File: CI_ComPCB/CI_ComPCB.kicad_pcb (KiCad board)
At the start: 2 copper layers, 101.6 x 86.4 mm, 52 parts, among them IC301 TPS63020DSJR, IC401 TPS54331DR, J101 Conn_01x01_Male, J301 Connector_Conn_01x02_Male, J302 Connector_Conn_01x02_Male, J401 Connector_Conn_01x02_Male, J402 Connector_Conn_01x02_Male, J501 RJ45_LED_Shielded, J502 RJ45_LED_Shielded, Q201 Transistor_FET_IRF9540N, U101 ESP32s

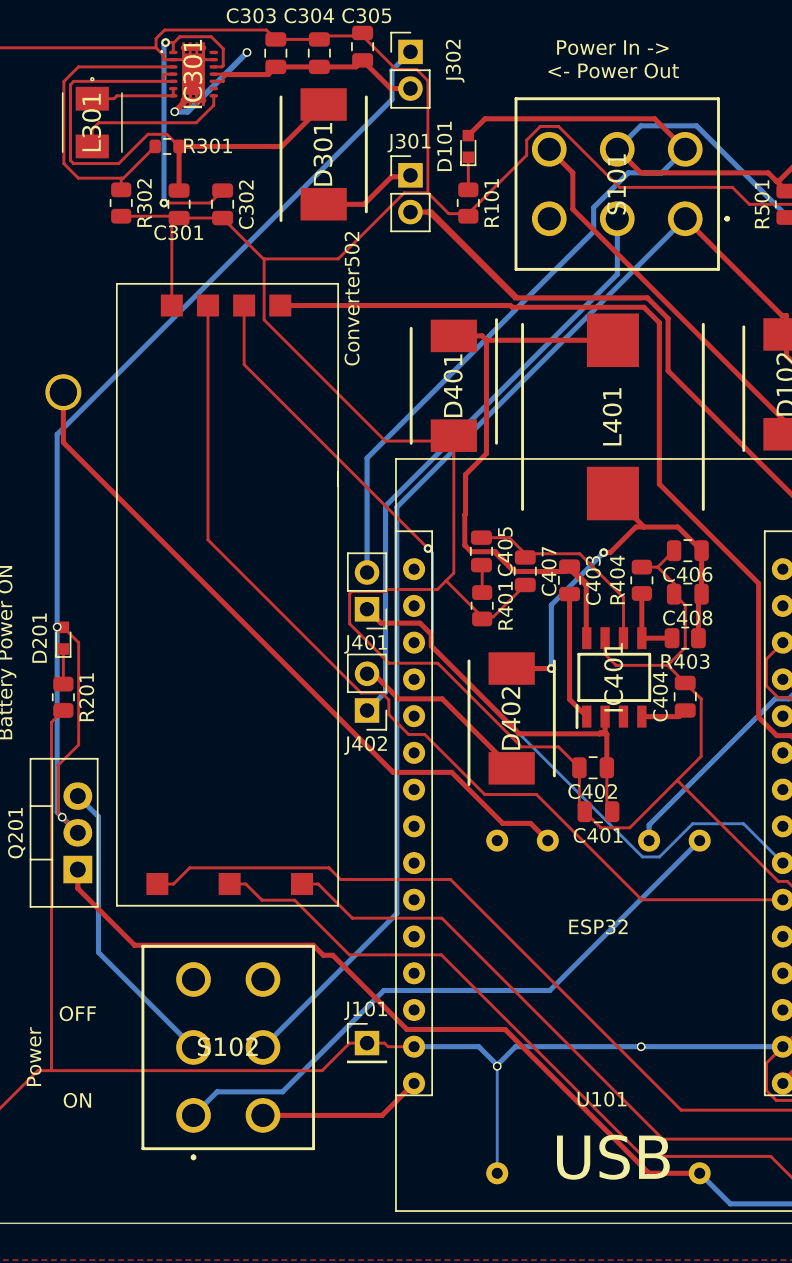
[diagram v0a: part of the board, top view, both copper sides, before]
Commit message: V1.1 board
Board is ready to print
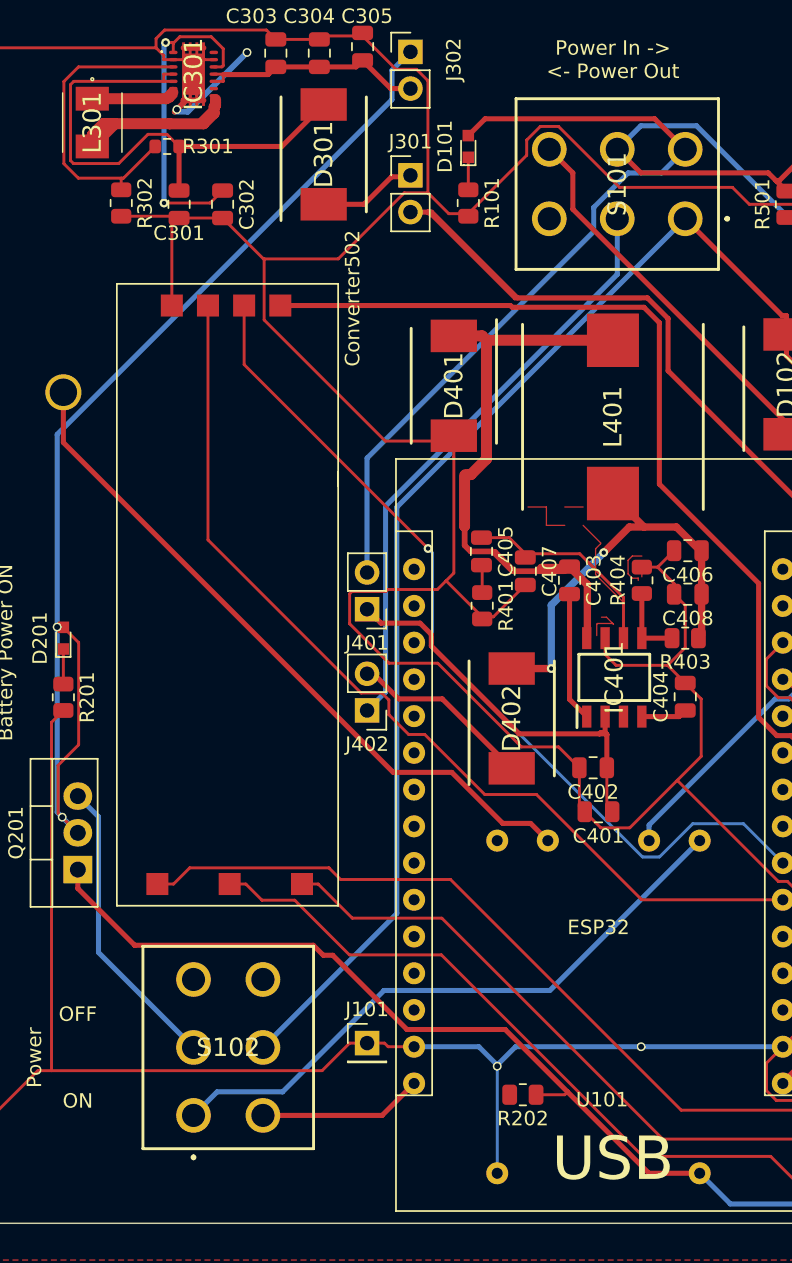
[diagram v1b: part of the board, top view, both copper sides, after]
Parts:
- added R202: 10k, Resistor_SMD:R_0805_2012Metric, F.Cu at (88.8, 151.6)
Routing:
- net Net-(IC301-Pad8): track 10.9 -> 32.9 mm
- net Net-(C403-Pad1): track 57.6 -> 74.4 mm
- net (no net): track 0.00 -> 11.1 mm
- net Net-(C405-Pad1): track 14.6 -> 21.4 mm
- net Net-(IC301-Pad6): track 6.18 -> 11.9 mm
- net Charger_IN: track 128.0 -> 130.2 mm
- net GND: track 448.1 -> 448.8 mm

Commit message: V1.1 Changed Diode for reprint
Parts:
- D102, D301, D401, D402: footprint SamacSys_Parts:DIOM8059X256N -> digikey-footprints:DO-214AC
- moved D402 2.00 mm to (89.7, 126.6)
- moved D401 1.29 mm to (83.7, 103.8)
- moved D301 0.97 mm to (74.8, 87.5)
- moved D102 0.40 mm to (107.2, 102.8)
- moved R404 0.21 mm to (97.1, 116.2)
- moved IC401 0.09 mm to (95.1, 122.8)
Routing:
- net GND: track 448.8 -> 433.6 mm, vias 6 -> 8
- net (no net): track 11.1 -> 0.00 mm
- net Net-(C405-Pad1): track 21.4 -> 14.2 mm
- net Net-(C403-Pad1): track 74.4 -> 80.0 mm
- net Net-(D402-Pad1): track 12.7 -> 14.6 mm
- net Net-(C301-Pad1): track 36.6 -> 35.4 mm
- net Net-(C401-Pad1): track 27.8 -> 28.4 mm
- net Charger_OUT: vias 2 -> 1

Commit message: converters debug
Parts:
- added Q501: Transistor_FET_IRF9540N-CI_ComPCB-cache, Package_TO_SOT_THT:TO-220-3_Vertical, F.Cu at (-2.06, 105.6)
- added Q502: Transistor_FET_IRF9540N-CI_ComPCB-cache, Package_TO_SOT_THT:TO-220-3_Vertical, F.Cu at (-2.06, 111.6)
- added R503: 10k, Resistor_SMD:R_0805_2012Metric, F.Cu at (8.46, 103.1)
- C303, C304, C305: value 100nF -> 10uf
- moved D301 40.7 mm to (52.6, 53.4), turned to 0 degrees
- moved C302 37.2 mm to (66.3, 52.9), turned to 0 degrees
- moved C301 31.3 mm to (58.4, 59.4), turned to 0 degrees
- moved R302 28.7 mm to (67.3, 61.9), turned to 0 degrees
- moved IC301 27.0 mm to (60.4, 54.6), turned to 0 degrees
- moved L301 26.3 mm to (52.7, 58.8), turned to 0 degrees
- moved C304 25.1 mm to (66.3, 55.9), turned to 0 degrees
- moved R301 24.6 mm to (58.2, 62.1)
- moved C305 22.7 mm to (67.3, 58.9), turned to 0 degrees
- moved C303 22.0 mm to (62.8, 59.4), turned to 0 degrees
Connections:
- D301 pad 2: Net-(C301-Pad1) -> Net-(C303-Pad1)
- IC301 pad 10: Net-(C303-Pad1) -> Net-(C301-Pad1)
- IC301 pad 11: Net-(C303-Pad1) -> Net-(C301-Pad1)
- IC301 pad 4: Net-(C301-Pad1) -> Net-(C303-Pad1)
- IC301 pad 5: Net-(C301-Pad1) -> Net-(C303-Pad1)
- J302 pad 2: Net-(C303-Pad1) -> Net-(C301-Pad1)
- J501 pad 1: B0 -> B1
- J501 pad 2: A0 -> A1
- J501 pad 3: Net-(J501-Pad3) -> Tx1
- J501 pad 6: Net-(J501-Pad6) -> Rx1
- J501 pad 7: EPower -> Net-(J501-Pad7)
- J502 pad 1: B1 -> B0
- J502 pad 2: A1 -> A0
- J502 pad 3: Net-(J501-Pad3) -> Net-(J502-Pad3)
- J502 pad 4: Net-(J501-Pad4) -> Net-(J502-Pad4)
- J502 pad 5: Net-(J501-Pad5) -> Net-(J502-Pad5)
- J502 pad 6: Net-(J501-Pad6) -> GPIO???
- J502 pad 7: EPower -> Net-(J502-Pad7)
- R301 pad 2: Net-(C301-Pad1) -> Net-(C303-Pad1)
- R501 pad 2: EPower -> Net-(J501-Pad7)
- R502 pad 2: EPower -> Net-(J502-Pad7)
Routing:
- net GND: track 433.6 -> 336.4 mm, vias 8 -> 6
- net Net-(C301-Pad1): track 35.4 -> 0.00 mm
- net Net-(IC301-Pad8): track 32.9 -> 0.00 mm
- net Net-(C302-Pad1): track 22.6 -> 0.00 mm, vias 2 -> 0
- net Net-(IC301-Pad3): track 22.1 -> 0.00 mm
- net Net-(C303-Pad1): track 19.8 -> 0.00 mm
- net Net-(IC301-Pad6): track 11.9 -> 0.00 mm
- net Net-(D301-Pad1): track 6.83 -> 0.00 mm
- net Charger_OUT: track 80.5 -> 76.7 mm
- net Buck_Converter_OUT: track 138.8 -> 137.4 mm

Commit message: switch
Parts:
- removed C401, C402: 10uF, Capacitor_SMD:C_0805_2012Metric
- removed C403: 100nF, Capacitor_SMD:C_0805_2012Metric
- removed C404: 8.2nF, Capacitor_SMD:C_0805_2012Metric
- removed C405: 1nF, Capacitor_SMD:C_0805_2012Metric
- removed C406, C408: 47uF, Capacitor_SMD:C_0805_2012Metric
- removed C407: 10pf, Capacitor_SMD:C_0805_2012Metric
- removed D101: LTST-C190GKT, digikey-footprints:LED_0603
- removed D102, D401, D402: SS34, digikey-footprints:DO-214AC
- removed IC401: TPS54331DR, SamacSys_Parts:SOIC127P600X175-8N
- removed J301, J302: Connector_Conn_01x02_Male, Connector_PinHeader_2.54mm:PinHeader_1x02_P2.54mm_Vertical
- removed L401: RLF12560T-7R8N8R2, SamacSys_Parts:INDPM128125X600N
- removed Q501, Q502: Transistor_FET_IRF9540N-CI_ComPCB-cache, Package_TO_SOT_THT:TO-220-3_Vertical
- removed R101: 680, Resistor_SMD:R_0805_2012Metric
- removed R401: 56.2k, Resistor_SMD:R_0805_2012Metric
- removed R403: 10.2k, Resistor_SMD:R_0805_2012Metric
- removed R404: 1.78k, Resistor_SMD:R_0805_2012Metric
- removed R503: 10k, Resistor_SMD:R_0805_2012Metric
- added D501: SS34, digikey-footprints:DO-214AC, F.Cu at (122.4, 171.1)
- J401, J402: value Connector_Conn_01x02_Male -> Connector_Conn_01x01_Male; footprint Connector_PinHeader_2.54mm:PinHeader_1x02_P2.54mm_Vertical -> Connector_PinHeader_2.54mm:PinHeader_1x01_P2.54mm_Vertical
- moved S103 103.1 mm to (57.8, 58.5)
- moved S102 91.9 mm to (42.5, 64.1)
- moved S101 77.2 mm to (27.6, 64.1), turned to 0 degrees
- moved J402 43.4 mm to (121.4, 124.7), turned to 0 degrees
- moved J401 39.4 mm to (116.8, 124.7), turned to 0 degrees
- moved C302 18.3 mm to (84.6, 52.4)
- moved C304 18.3 mm to (84.6, 55.4)
- moved C303 18.3 mm to (81.1, 58.9)
- moved D301 18.3 mm to (70.9, 52.9)
- moved C301 18.3 mm to (76.7, 58.9)
- moved C305 18.3 mm to (85.6, 58.4)
- moved IC301 18.3 mm to (78.6, 54.1)
- moved L301 18.3 mm to (71.0, 58.3)
- moved R301 18.3 mm to (76.5, 61.6)
- moved R302 18.3 mm to (85.6, 61.4)
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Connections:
- J401 pad 1: Net-(C401-Pad1) -> Buck_IN
- J501 pad 3: Tx1 -> TX1
- J501 pad 6: Rx1 -> RX1
- J501 pad 7: Net-(J501-Pad7) -> EPower
- J502 pad 3: Net-(J502-Pad3) -> TX1
- J502 pad 6: GPIO??? -> RX1
- R501 pad 2: Net-(J501-Pad7) -> EPower
- U101 pad D13: Net-(U101-PadD13) -> RX1
- U101 pad D14: Net-(U101-PadD14) -> TX1
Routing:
- net GND: track 336.4 -> 0.00 mm, vias 6 -> 0
- net Sheild: track 182.9 -> 0.00 mm
- net EPower: track 140.3 -> 0.00 mm, vias 1 -> 0
- net Buck_Converter_OUT: track 137.4 -> 0.00 mm
- net Vin: track 136.3 -> 0.00 mm
- net Charger_IN: track 130.2 -> 0.00 mm
- net Net-(J501-Pad3): track 96.6 -> 0.00 mm, vias 1 -> 0
- net 3.3V: track 92.7 -> 0.00 mm
- net Net-(J501-Pad5): track 85.3 -> 0.00 mm
- net Net-(C403-Pad1): track 80.0 -> 0.00 mm
- net Charger_OUT: track 76.7 -> 0.00 mm, vias 1 -> 0
- net Net-(J501-Pad6): track 70.7 -> 0.00 mm, vias 1 -> 0
- net Net-(J501-Pad4): track 69.7 -> 0.00 mm
- net RX2: track 66.9 -> 0.00 mm
- net B1: track 64.5 -> 0.00 mm
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- removed copper zone on F.Cu, net GND
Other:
- board text removed: "Battery"
- board text removed: "Charging"
- board text removed: "OFF"
- board text removed: "ON"
- board text removed: "Power"
- board text removed: "Power In -> <- Power Out"
- board text removed: "Supplying"

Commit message: switch
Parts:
- added C401: 10uF, Capacitor_SMD:C_0805_2012Metric, F.Cu at (188.8, 88.9)
- added C402: 10uF, Capacitor_SMD:C_0805_2012Metric, F.Cu at (188.8, 91.9)
- added C403: 100nF, Capacitor_SMD:C_0805_2012Metric, F.Cu at (186.4, 78.1)
- added C404: 8.2nF, Capacitor_SMD:C_0805_2012Metric, F.Cu at (194.5, 83.7)
- added C405: 1nF, Capacitor_SMD:C_0805_2012Metric, F.Cu at (191.0, 74.6)
- added C406: 47uF, Capacitor_SMD:C_0805_2012Metric, F.Cu at (177.2, 86.3)
- added C407: 10pf, Capacitor_SMD:C_0805_2012Metric, F.Cu at (186.3, 73.6)
- added C408: 47uF, Capacitor_SMD:C_0805_2012Metric, F.Cu at (177.2, 81.7)
- added D101: LTST-C190GKT, digikey-footprints:LED_0603, F.Cu at (192.6, 93.0)
- added D102: SS34, digikey-footprints:DO-214AC, F.Cu at (102.1, 85.3)
- added D401: SS34, digikey-footprints:DO-214AC, F.Cu at (183.4, 83.2)
- added D402: SS34, digikey-footprints:DO-214AC, F.Cu at (179.8, 90.9)
- added IC401: TPS54331DR, SamacSys_Parts:SOIC127P600X175-8N, F.Cu at (190.5, 82.7)
- added J301: Connector_Conn_01x01_Male, Connector_PinHeader_2.54mm:PinHeader_1x01_P2.54mm_Vertical, F.Cu at (69.1, 48.2)
- added J302: Connector_Conn_01x01_Male, Connector_PinHeader_2.54mm:PinHeader_1x01_P2.54mm_Vertical, F.Cu at (64.5, 48.7)
- added J303: Connector_Conn_01x01_Male, Connector_PinHeader_2.54mm:PinHeader_1x01_P2.54mm_Vertical, F.Cu at (69.1, 44.1)
- added L401: RLF12560T-7R8N8R2, SamacSys_Parts:INDPM128125X600N, F.Cu at (176.0, 72.1)
- added R101: 680, Resistor_SMD:R_0805_2012Metric, F.Cu at (192.5, 89.2)
- added R401: 56.2k, Resistor_SMD:R_0805_2012Metric, F.Cu at (186.3, 70.0)
- added R403: 10.2k, Resistor_SMD:R_0805_2012Metric, F.Cu at (191.0, 69.4)
- added R404: 1.78k, Resistor_SMD:R_0805_2012Metric, F.Cu at (186.4, 66.5)
- HW-201: moved to F.Cu
- S101, S102: value CS22BNW03 -> L202021MA04QE; footprint SamacSys_Parts:CS22BNW03 -> SamacSys_Parts:L202021MA04QE
- S103: value CS12ANW03 -> L102021ML04Q; footprint SamacSys_Parts:CS12ANW03 -> SamacSys_Parts:L102011ML04Q
- moved D501 95.5 mm to (105.2, 77.1), turned to 180 degrees
- moved S102 79.9 mm to (49.3, 143.7)
- moved J401 77.9 mm to (189.0, 95.4), turned to 90 degrees
- moved J501 73.5 mm to (126.5, 153.9), turned to 180 degrees
- moved J502 73.3 mm to (119.9, 80.7), turned to 0 degrees
- moved R501 69.6 mm to (134.6, 153.9), turned to 270 degrees
- moved Holder201 69.1 mm to (65.5, 110.2), turned to 0 degrees
- moved J402 68.5 mm to (183.4, 95.4), turned to 90 degrees
- moved R502 66.5 mm to (112.2, 84.2), turned to 90 degrees
- moved Converter502 62.7 mm to (138.7, 98.0)
- moved S101 56.9 mm to (82.6, 78.6), turned to 270 degrees
- moved S103 50.6 mm to (45.7, 107.6), turned to 180 degrees
- moved C302 35.9 mm to (48.7, 51.2), turned to 270 degrees
- moved R302 34.7 mm to (51.7, 53.8), turned to 180 degrees
- moved C305 26.4 mm to (59.4, 55.3), turned to 90 degrees
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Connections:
- C301 pad 1: Net-(C301-Pad1) -> Charger_OUT
- D301 pad 1: Net-(D301-Pad1) -> Buck_Converter_OUT
- IC301 pad 10: Net-(C301-Pad1) -> Charger_OUT
- IC301 pad 11: Net-(C301-Pad1) -> Charger_OUT
- S103 pad 2: Vin -> Charger_IN
- S103 pad 3: Charger_IN -> Vin
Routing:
- net GND: track 0.00 -> 95.3 mm, vias 0 -> 31
- net Net-(C406-Pad1): track 0.00 -> 48.3 mm
- net Net-(C303-Pad1): track 0.00 -> 27.2 mm
- net Charger_OUT: track 0.00 -> 20.9 mm
- net Net-(C403-Pad1): track 0.00 -> 17.2 mm
- net Net-(IC401-Pad5): track 0.00 -> 16.1 mm
- net Net-(C302-Pad1): track 0.00 -> 14.4 mm
- net Net-(IC301-Pad6): track 0.00 -> 12.6 mm
- net Net-(IC301-Pad3): track 0.00 -> 11.0 mm
- net Buck_IN: track 0.00 -> 10.4 mm
- net Net-(C405-Pad1): track 0.00 -> 9.03 mm
- net Net-(C403-Pad2): track 0.00 -> 7.28 mm
- net Net-(C405-Pad2): track 0.00 -> 5.26 mm
- net Buck_Out: track 0.00 -> 5.20 mm
- net Net-(IC301-Pad8): track 0.00 -> 5.03 mm
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- added copper zone on B.Cu, net GND
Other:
- board text removed: "Battery Power ON"

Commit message: Ready to Build
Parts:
- removed D101: LTST-C190GKT, digikey-footprints:LED_0603
- removed D102: SS34, digikey-footprints:DO-214AC
- removed R101: 680, Resistor_SMD:R_0805_2012Metric
- removed S101: L202021MA04QE, SamacSys_Parts:L202021MA04QE
- removed S103: L102021ML04Q, SamacSys_Parts:L102011ML04Q
- added D601: LTST-C190GKT, digikey-footprints:LED_0603, F.Cu at (114.8, 110.7)
- added D602: LTST-C190GKT, digikey-footprints:LED_0603, F.Cu at (115.6, 78.2)
- added D603: 1N4007, digikey-footprints:DO-214AC, F.Cu at (121.6, 114.2)
- added D604: 1N4007, digikey-footprints:DO-214AC, F.Cu at (121.6, 81.2)
- added D605: SS34, digikey-footprints:DO-214AC, F.Cu at (137.6, 91.4)
- added D606: LTST-C190GKT, digikey-footprints:LED_0603, F.Cu at (119.9, 103.6)
- added J403: Conn_01x01_Male, Connector_PinHeader_2.54mm:PinHeader_1x01_P2.54mm_Vertical, F.Cu at (162.0, 120.8)
- added J601: Conn_01x02_Male, Connector_PinHeader_2.54mm:PinHeader_1x02_P2.54mm_Vertical, F.Cu at (132.6, 120.8)
- added J602: Conn_01x02_Male, Connector_PinHeader_2.54mm:PinHeader_1x02_P2.54mm_Vertical, F.Cu at (133.1, 88.8)
- added J603: Conn_01x03_Male, Connector_PinHeader_2.54mm:PinHeader_1x03_P2.54mm_Vertical, F.Cu at (132.6, 126.9)
- added J604: Conn_01x03_Male, Connector_PinHeader_2.54mm:PinHeader_1x03_P2.54mm_Vertical, F.Cu at (133.1, 95.0)
- added J605: Conn_01x02_Male, Connector_PinHeader_2.54mm:PinHeader_1x02_P2.54mm_Vertical, F.Cu at (173.5, 155.1)
- added K601: SRD-05VDC-SL-C, SRD-05VDC-SL-C:RELAY_SRD-05VDC-SL-C, F.Cu at (118.9, 125.4)
- added K602: SRD-05VDC-SL-C, SRD-05VDC-SL-C:RELAY_SRD-05VDC-SL-C, F.Cu at (118.3, 92.4)
- added Q601: 2N3904, digikey-footprints:TO-92-3, F.Cu at (109.2, 114.2)
- added Q602: 2N3904, digikey-footprints:TO-92-3, F.Cu at (109.7, 81.7)
- added R601: 5.6k, Resistor_SMD:R_0805_2012Metric, F.Cu at (110.3, 106.6)
- added R602: 5.6k, Resistor_SMD:R_0805_2012Metric, F.Cu at (110.2, 75.6)
- added R603: 1k, Resistor_SMD:R_0805_2012Metric, F.Cu at (122.4, 109.7)
- added R604: 1k, Resistor_SMD:R_0805_2012Metric, F.Cu at (121.9, 77.1)
- added R605: 680, Resistor_SMD:R_0805_2012Metric, F.Cu at (124.0, 103.6)
- added R606: 11k, Resistor_SMD:R_0805_2012Metric, F.Cu at (180.2, 155.9)
- added R607: 29k, Resistor_SMD:R_0805_2012Metric, F.Cu at (177.9, 152.3)
- C404: footprint Capacitor_SMD:C_0805_2012Metric -> Capacitor_SMD:C_0603_1608Metric
- J402: value Connector_Conn_01x01_Male -> Conn_01x02_Male; footprint Connector_PinHeader_2.54mm:PinHeader_1x01_P2.54mm_Vertical -> Connector_PinHeader_2.54mm:PinHeader_1x02_P2.54mm_Vertical
- moved C302 124.7 mm to (170.2, 79.8), turned to 90 degrees
- moved R302 117.9 mm to (167.2, 77.1), turned to 0 degrees
- moved IC301 117.7 mm to (165.8, 82.5), turned to 180 degrees
- moved R301 109.1 mm to (163.2, 74.6), turned to 180 degrees
- moved L301 104.8 mm to (159.0, 82.6), turned to 270 degrees
- moved C305 102.1 mm to (159.5, 75.6), turned to 270 degrees
- moved C301 98.7 mm to (154.4, 85.8), turned to 90 degrees
- moved C304 96.1 mm to (156.4, 75.6), turned to 270 degrees
- moved J302 96.0 mm to (154.4, 82.2), turned to 0 degrees
- moved J303 91.4 mm to (149.8, 86.8), turned to 0 degrees
- moved C303 90.2 mm to (153.4, 75.6), turned to 270 degrees
- moved J301 87.8 mm to (149.8, 82.7), turned to 0 degrees
- moved D301 84.1 mm to (149.8, 77.1), turned to 90 degrees
- moved Q201 81.3 mm to (137.6, 139.6)
- moved S102 79.2 mm to (128.0, 152.3), turned to 90 degrees
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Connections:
- D402 pad 1: Buck_Out -> Net-(D402-Pad1)
- J402 pad 1: Buck_Out -> Vin
- U101 pad D25: Net-(U101-PadD25) -> Ch3
- U101 pad D32: Net-(U101-PadD32) -> Ch1
- U101 pad D33: Net-(U101-PadD33) -> Ch2
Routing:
- net GND: track 95.3 -> 397.9 mm, vias 31 -> 58
- net Sheild: track 0.00 -> 168.0 mm, vias 0 -> 2
- net EPower: track 0.00 -> 165.3 mm, vias 0 -> 3
- net TX1: track 0.00 -> 145.1 mm
- net Net-(HW-201-Pad2): track 0.00 -> 139.5 mm
- net Vin: track 0.00 -> 138.5 mm
- net RX1: track 0.00 -> 127.9 mm, vias 0 -> 1
- net Buck_IN: track 10.4 -> 96.2 mm
- net Charger_OUT: track 20.9 -> 103.6 mm, vias 0 -> 1
- net Buck_Converter_OUT: track 3.59 -> 82.2 mm, vias 0 -> 1
- net Charger_IN: track 0.00 -> 72.6 mm
- net 3.3V: track 0.00 -> 72.6 mm
- net Ch2: track 0.00 -> 70.5 mm, vias 0 -> 1
- net TX2: track 0.00 -> 64.8 mm, vias 0 -> 1
- net RX2: track 0.00 -> 59.6 mm, vias 0 -> 1
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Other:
- board size 101.6 x 86.4 mm -> 121.9 x 86.4 mm
- board text added: "Battery ON"
- board text added: "CI_ComPCB V1.2 Innovive"
- board text added: "Ch3 diss"
- board text added: "Charging"
- board text added: "GND"
- board text added: "In/Out"
- board text added: "NC"
- board text added: "NO"
- board text added: "OFF ----- ON"
- board text added: "Vin"
- board text added: "Vin disconnect"
- board text added: "Vout"
- board text added: "Vout Diss"
- board text removed: "CI_ComPCB V1.1 Innovive"
